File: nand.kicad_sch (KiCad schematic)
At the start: 1 part

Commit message: write some things down
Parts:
- U1: renamed from U?; value MCIMX6YxxVMxxxx -> MCIMX6Y2DVM09AB; Manufacturer (none) -> NXP; MfgPartNo (none) -> MCIMX6Y2DVM09AB; Vendor (none) -> Digi-Key; VendorPartNo (none) -> 568-14995-ND
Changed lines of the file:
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@@
   (symbol (lib_id "catfood:MCIMX6YxxVMxxxx") (at 71.12 63.5 0) (unit 10)
     (in_bom yes) (on_board yes) (fields_autoplaced)
-    (property "Reference" "U?" (id 0) (at 71.12 31.75 0))
-    (property "Value" "MCIMX6YxxVMxxxx" (id 1) (at 71.12 34.29 0))
+    (property "Reference" "U1" (id 0) (at 71.12 31.75 0))
+    (property "Value" "MCIMX6Y2DVM09AB" (id 1) (at 71.12 34.29 0))
     (property "Footprint" "" (id 2) (at 60.96 44.45 0)
       (effects (font (size 1.27 1.27)) hide)
@@
       (effects (font (size 1.27 1.27)) hide)
     )
+    (property "Manufacturer" "NXP" (id 4) (at 71.12 41.91 0)
+      (effects (font (size 1.27 1.27)) hide)
+    )
+    (property "MfgPartNo" "MCIMX6Y2DVM09AB" (id 5) (at 71.12 44.45 0)
+      (effects (font (size 1.27 1.27)) hide)
+    )
+    (property "Vendor" "Digi-Key" (id 6) (at 71.12 46.99 0)
+      (effects (font (size 1.27 1.27)) hide)
+    )
+    (property "VendorPartNo" "568-14995-ND" (id 7) (at 71.12 49.53 0)
+      (effects (font (size 1.27 1.27)) hide)
+    )

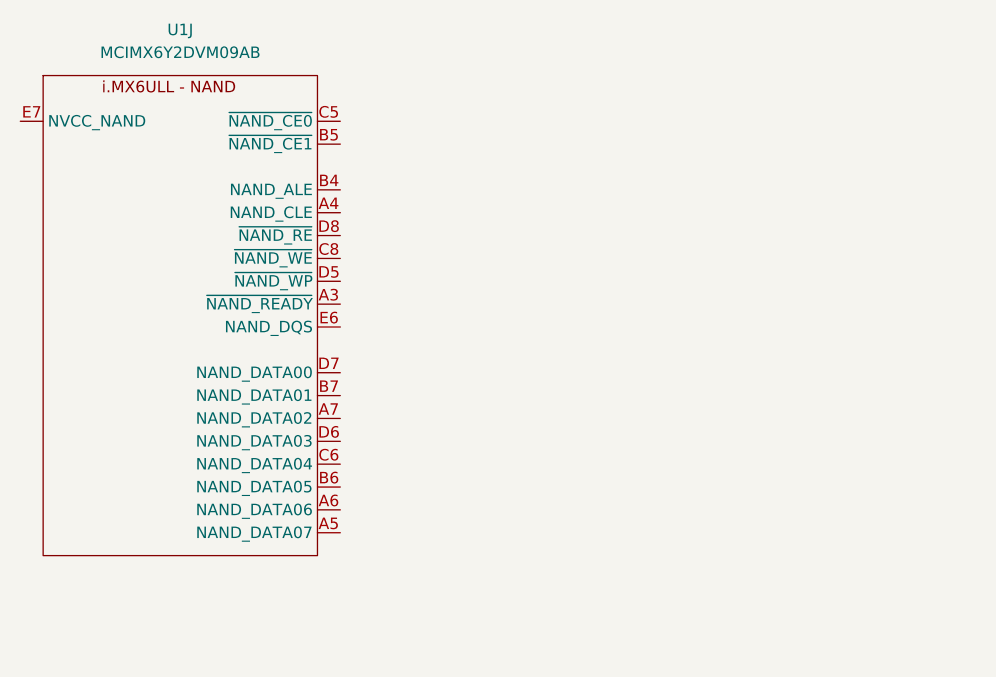
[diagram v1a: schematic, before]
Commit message: NAND symbol
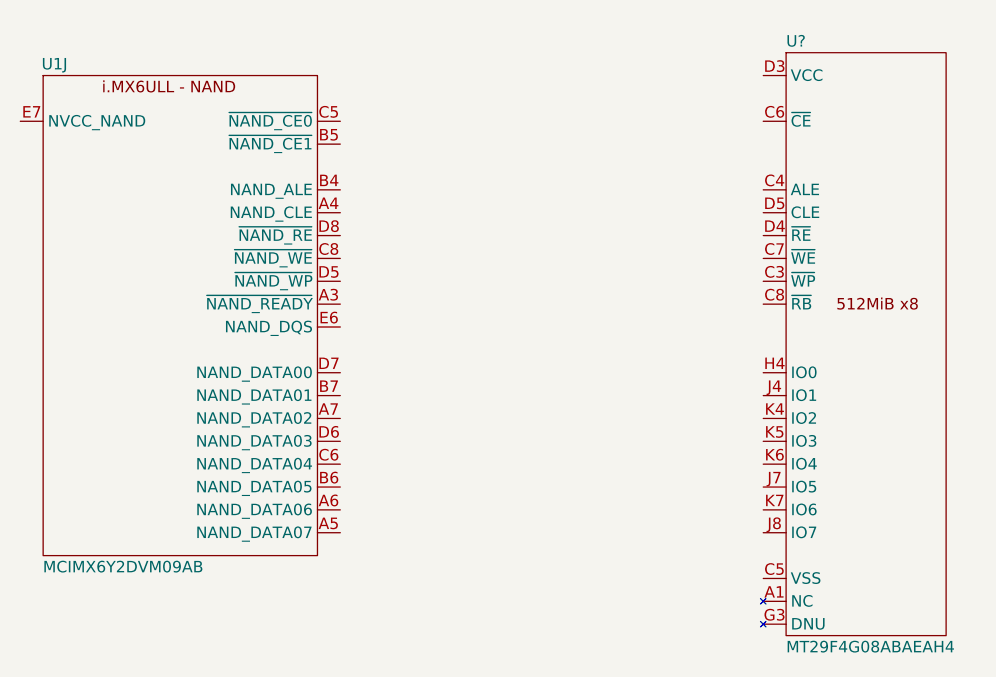
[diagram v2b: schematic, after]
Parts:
- added U?: MT29F4G08ABAEAH4, symbol catfood:MT29F4G08ABAEAH4
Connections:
- new net: U?.A1 (NC), U?.A10 (NC), U?.A2 (NC), U?.A9 (NC), U?.B1 (NC), U?.B10 (NC), U?.B9 (NC), U?.D6 (NC), U?.D7 (NC), U?.D8 (NC), U?.E3 (NC), U?.E4 (NC), U?.E5 (NC), U?.E6 (NC), U?.E7 (NC), U?.E8 (NC), U?.F3 (NC), U?.F4 (NC), U?.F5 (NC), U?.F6 (NC), U?.F8 (NC), U?.G6 (NC), U?.G7 (NC), U?.H3 (NC), U?.H5 (NC), U?.H6 (NC), U?.H7 (NC), U?.J3 (NC), U?.J5 (NC), U?.L1 (NC), U?.L10 (NC), U?.L2 (NC), U?.L9 (NC), U?.M1 (NC), U?.M10 (NC), U?.M2 (NC), U?.M9 (NC)
- new net: U?.G3 (DNU), U?.G5 (DNU), U?.G8 (DNU)
- new net VCC: U?.D3 (VCC), U?.G4 (VCC), U?.H8 (VCC), U?.J6 (VCC)
- new net VSS: U?.C5 (VSS), U?.F7 (VSS), U?.K3 (VSS), U?.K8 (VSS)
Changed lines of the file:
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@@
   )
   (symbol (lib_id "catfood:MCIMX6YxxVMxxxx") (at 71.12 63.5 0) (unit 10)
-    (in_bom yes) (on_board yes) (fields_autoplaced)
-    (property "Reference" "U1" (id 0) (at 71.12 31.75 0))
-    (property "Value" "MCIMX6Y2DVM09AB" (id 1) (at 71.12 34.29 0))
+    (in_bom yes) (on_board yes)
+    (property "Reference" "U1" (id 0) (at 57.15 35.56 0))
+    (property "Value" "MCIMX6Y2DVM09AB" (id 1) (at 64.77 91.44 0))
     (property "Footprint" "" (id 2) (at 60.96 44.45 0)
       (effects (font (size 1.27 1.27)) hide)
@@
     (pin "N17")
   )
+  (symbol (lib_id "catfood:MT29F4G08ABAEAH4") (at 146.05 43.18 0) (unit 1)
+    (in_bom yes) (on_board yes)
+    (property "Reference" "U?" (id 0) (at 138.43 33.02 0)
+      (effects (font (size 1.27 1.27)) (justify left))
+    )
+    (property "Value" "MT29F4G08ABAEAH4" (id 1) (at 138.43 100.33 0)
+      (effects (font (size 1.27 1.27)) (justify left))
+    )
+    (property "Footprint" "" (id 2) (at 135.89 95.25 0)
+      (effects (font (size 1.27 1.27)) hide)
+    )
+    (property "Datasheet" "" (id 3) (at 135.89 95.25 0)
+      (effects (font (size 1.27 1.27)) hide)
+    )
+    (pin "A1")
+    (pin "A10")
+    (pin "A2")
+    (pin "A9")
+    (pin "B1")
+    (pin "B10")
+    (pin "B9")
+    (pin "C3")
+    (pin "C4")
+    (pin "C5")
+    (pin "C6")
+    (pin "C7")
+    (pin "C8")
+    (pin "D3")
+    (pin "D4")
+    (pin "D5")
+    (pin "D6")
+    (pin "D7")
+    (pin "D8")
+    (pin "E3")
+    (pin "E4")
+    (pin "E5")
+    (pin "E6")
+    (pin "E7")
+    (pin "E8")
+    (pin "F3")
+    (pin "F4")
+    (pin "F5")
+    (pin "F6")
+    (pin "F7")
+    (pin "F8")
+    (pin "G3")
+    (pin "G4")
+    (pin "G5")
+    (pin "G6")
+    (pin "G7")
+    (pin "G8")
+    (pin "H3")
+    (pin "H4")
+    (pin "H5")
+    (pin "H6")
+    (pin "H7")
+    (pin "H8")
+    (pin "J3")
+    (pin "J4")
+    (pin "J5")
+    (pin "J6")
+    (pin "J7")
+    (pin "J8")
+    (pin "K3")
+    (pin "K4")
+    (pin "K5")
+    (pin "K6")
+    (pin "K7")
+    (pin "K8")
+    (pin "L1")
+    (pin "L10")
+    (pin "L2")
+    (pin "L9")
+    (pin "M1")
+    (pin "M10")
+    (pin "M2")
+    (pin "M9")
+  )
 )

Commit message: NAND
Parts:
- added C?: 18pF 0402, symbol Device:C_Small
- added C? (x4): 0.1uF 0402, symbol Device:C_Small
- added C?: 0.22uF 0402, symbol Device:C_Small
- added C?: 4.7uF 0603, symbol Device:C_Small
- added R? (x2): 10k 0402, symbol Device:R_Small
- added R? (x2): 10R 0402, symbol Device:R_Small
- added R?: 0R 0402, symbol Device:R_Small
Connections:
- net VCC: now also U1.E7 (NVCC_NAND), C?.1, C?.1, C?.1, C?.1, C?.1, C?.1, R?.1, R?.1
- net NAND_nREADY: now reaches U1.A3 (~{NAND_READY})
- net NAND_nREADY: now also U?.C8 (~{RB}), R?.2
- net NAND_CLE: now reaches U1.A4 (NAND_CLE)
- net NAND_CLE: now also U?.D5 (CLE)
- net at U1.A5 (NAND_DATA07): now also U?.J8 (IO7)
- net at U1.A6 (NAND_DATA06): now also U?.K7 (IO6)
- net at U1.A7 (NAND_DATA02): now also U?.K4 (IO2)
- net at U1.B4 (NAND_ALE): now also R?.1
- net at U1.B6 (NAND_DATA05): now also U?.J7 (IO5)
- net at U1.B7 (NAND_DATA01): now also U?.J4 (IO1)
- net NAND_nCE0: now reaches U1.C5 (~{NAND_CE0})
- net NAND_nCE0: now also U?.C6 (~{CE}), R?.2
- net at U1.C6 (NAND_DATA04): now also U?.K6 (IO4)
- net at U1.C8 (~{NAND_WE}): now also R?.1
- net NAND_nWP: now reaches U1.D5 (~{NAND_WP})
- net NAND_nWP: now also U?.C3 (~{WP})
- net at U1.D6 (NAND_DATA03): now also U?.K5 (IO3)
- net at U1.D7 (NAND_DATA00): now also U?.H4 (IO0)
- net at U1.D8 (~{NAND_RE}): now also R?.1
- net NAND_ALE: now reaches U?.C4 (ALE)
- net NAND_ALE: now also R?.2
- net NAND_nWE: now reaches U?.C7 (~{WE})
- net NAND_nWE: now also R?.2
- net NAND_nRE: now reaches U?.D4 (~{RE})
- net NAND_nRE: now also C?.1, R?.2
- net VSS renamed GND
- net GND: now also C?.2, C?.2, C?.2, C?.2, C?.2, C?.2, C?.2
- no-connect marks 0 -> 2
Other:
- moved on the sheet: U1J, U?

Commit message: Annotation
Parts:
- gave numbers to parts that had none: 13
- renumbered U1 to U4
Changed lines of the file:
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@@
   (symbol (lib_id "Device:C_Small") (at 113.665 133.985 0) (unit 1)
     (in_bom yes) (on_board yes) (fields_autoplaced)
-    (property "Reference" "C?" (id 0) (at 116.205 132.7212 0)
+    (property "Reference" "C68" (id 0) (at 116.205 132.7212 0)
       (effects (font (size 1.27 1.27)) (justify left))
     )
@@
   (symbol (lib_id "Device:C_Small") (at 210.185 62.865 0) (unit 1)
     (in_bom yes) (on_board yes) (fields_autoplaced)
-    (property "Reference" "C?" (id 0) (at 212.725 61.6012 0)
+    (property "Reference" "C73" (id 0) (at 212.725 61.6012 0)
       (effects (font (size 1.27 1.27)) (justify left))
     )
@@
   (symbol (lib_id "power:GND") (at 224.155 136.525 0) (unit 1)
     (in_bom yes) (on_board yes) (fields_autoplaced)
-    (property "Reference" "#PWR?" (id 0) (at 224.155 142.875 0)
+    (property "Reference" "#PWR089" (id 0) (at 224.155 142.875 0)
       (effects (font (size 1.27 1.27)) hide)
     )
@@
   (symbol (lib_id "Device:C_Small") (at 27.94 81.915 0) (unit 1)
     (in_bom yes) (on_board yes) (fields_autoplaced)
-    (property "Reference" "C?" (id 0) (at 30.48 80.6512 0)
+    (property "Reference" "C67" (id 0) (at 30.48 80.6512 0)
       (effects (font (size 1.27 1.27)) (justify left))
     )
@@
   (symbol (lib_id "Device:C_Small") (at 193.675 62.865 0) (unit 1)
     (in_bom yes) (on_board yes) (fields_autoplaced)
-    (property "Reference" "C?" (id 0) (at 196.215 61.6012 0)
+    (property "Reference" "C72" (id 0) (at 196.215 61.6012 0)
       (effects (font (size 1.27 1.27)) (justify left))
     )
@@
   (symbol (lib_id "Device:R_Small") (at 118.745 71.755 0) (unit 1)
     (in_bom yes) (on_board yes) (fields_autoplaced)
-    (property "Reference" "R?" (id 0) (at 121.285 70.4849 0)
+    (property "Reference" "R26" (id 0) (at 121.285 70.4849 0)
       (effects (font (size 1.27 1.27)) (justify left))
     )
@@
   (symbol (lib_id "power:GND") (at 210.185 67.945 0) (unit 1)
     (in_bom yes) (on_board yes) (fields_autoplaced)
-    (property "Reference" "#PWR?" (id 0) (at 210.185 74.295 0)
+    (property "Reference" "#PWR088" (id 0) (at 210.185 74.295 0)
       (effects (font (size 1.27 1.27)) hide)
     )
@@
   (symbol (lib_id "power:GND") (at 113.665 140.335 0) (unit 1)
     (in_bom yes) (on_board yes) (fields_autoplaced)
-    (property "Reference" "#PWR?" (id 0) (at 113.665 146.685 0)
+    (property "Reference" "#PWR085" (id 0) (at 113.665 146.685 0)
       (effects (font (size 1.27 1.27)) hide)
     )
@@
   (symbol (lib_id "Device:C_Small") (at 144.145 62.865 0) (unit 1)
     (in_bom yes) (on_board yes) (fields_autoplaced)
-    (property "Reference" "C?" (id 0) (at 146.685 61.6012 0)
+    (property "Reference" "C69" (id 0) (at 146.685 61.6012 0)
       (effects (font (size 1.27 1.27)) (justify left))
     )
@@
   (symbol (lib_id "catfood:MCIMX6YxxVMxxxx") (at 60.325 98.425 0) (unit 10)
     (in_bom yes) (on_board yes)
-    (property "Reference" "U1" (id 0) (at 46.355 70.485 0))
+    (property "Reference" "U4" (id 0) (at 46.355 70.485 0))
     (property "Value" "MCIMX6Y2DVM09AB" (id 1) (at 53.975 126.365 0))
     (property "Footprint" "" (id 2) (at 50.165 79.375 0)
@@
   (symbol (lib_id "Device:R_Small") (at 94.615 92.075 90) (unit 1)
     (in_bom yes) (on_board yes)
-    (property "Reference" "R?" (id 0) (at 92.075 90.805 90)
+    (property "Reference" "R24" (id 0) (at 92.075 90.805 90)
       (effects (font (size 0.8 0.8)))
     )
@@
   (symbol (lib_id "catfood:VDD_3V3") (at 144.145 56.515 0) (unit 1)
     (in_bom yes) (on_board yes) (fields_autoplaced)
-    (property "Reference" "#PWR?" (id 0) (at 144.145 60.325 0)
+    (property "Reference" "#PWR087" (id 0) (at 144.145 60.325 0)
       (effects (font (size 1.27 1.27)) hide)
     )
@@
   (symbol (lib_id "Device:R_Small") (at 94.615 89.535 90) (unit 1)
     (in_bom yes) (on_board yes)
-    (property "Reference" "R?" (id 0) (at 92.075 88.265 90)
+    (property "Reference" "R23" (id 0) (at 92.075 88.265 90)
       (effects (font (size 0.8 0.8)))
     )
@@
   (symbol (lib_id "catfood:MT29F4G08ABAEAH4") (at 238.125 78.105 0) (unit 1)
     (in_bom yes) (on_board yes)
-    (property "Reference" "U?" (id 0) (at 230.505 67.945 0)
+    (property "Reference" "U7" (id 0) (at 230.505 67.945 0)
       (effects (font (size 1.27 1.27)) (justify left))
     )
@@
   (symbol (lib_id "Device:C_Small") (at 177.165 62.865 0) (unit 1)
     (in_bom yes) (on_board yes) (fields_autoplaced)
-    (property "Reference" "C?" (id 0) (at 179.705 61.6012 0)
+    (property "Reference" "C71" (id 0) (at 179.705 61.6012 0)
       (effects (font (size 1.27 1.27)) (justify left))
     )
@@
   (symbol (lib_id "Device:C_Small") (at 160.655 62.865 0) (unit 1)
     (in_bom yes) (on_board yes) (fields_autoplaced)
-    (property "Reference" "C?" (id 0) (at 163.195 61.6012 0)
+    (property "Reference" "C70" (id 0) (at 163.195 61.6012 0)
       (effects (font (size 1.27 1.27)) (justify left))
     )
@@
   (symbol (lib_id "catfood:VDD_3V3") (at 118.745 64.135 0) (unit 1)
     (in_bom yes) (on_board yes) (fields_autoplaced)
-    (property "Reference" "#PWR?" (id 0) (at 118.745 67.945 0)
+    (property "Reference" "#PWR086" (id 0) (at 118.745 67.945 0)
       (effects (font (size 1.27 1.27)) hide)
     )
@@
   (symbol (lib_id "Device:R_Small") (at 104.775 71.755 0) (unit 1)
     (in_bom yes) (on_board yes) (fields_autoplaced)
-    (property "Reference" "R?" (id 0) (at 107.315 70.4849 0)
+    (property "Reference" "R25" (id 0) (at 107.315 70.4849 0)
       (effects (font (size 1.27 1.27)) (justify left))
     )
@@
   (symbol (lib_id "Device:R_Small") (at 94.615 84.455 90) (unit 1)
     (in_bom yes) (on_board yes)
-    (property "Reference" "R?" (id 0) (at 92.075 83.185 90)
+    (property "Reference" "R22" (id 0) (at 92.075 83.185 90)
       (effects (font (size 0.8 0.8)))
     )
@@
   (symbol (lib_id "catfood:VDD_3V3") (at 27.94 74.93 0) (unit 1)
     (in_bom yes) (on_board yes) (fields_autoplaced)
-    (property "Reference" "#PWR?" (id 0) (at 27.94 78.74 0)
+    (property "Reference" "#PWR083" (id 0) (at 27.94 78.74 0)
       (effects (font (size 1.27 1.27)) hide)
     )
@@
   (symbol (lib_id "power:GND") (at 27.94 89.535 0) (unit 1)
     (in_bom yes) (on_board yes) (fields_autoplaced)
-    (property "Reference" "#PWR?" (id 0) (at 27.94 95.885 0)
-      (effects (font (size 1.27 1.27)) hide)
-    )
+    (property "Reference" "#PWR084" (id 0) (at 27.94 95.885 0)
+      (effects (font (size 1.27 1.27)) hide)
+    )
